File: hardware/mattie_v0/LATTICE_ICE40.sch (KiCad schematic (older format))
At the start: 4 parts

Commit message: update
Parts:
- gave numbers to parts that had none: 1
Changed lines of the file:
@@
 $Descr A4 11693 8268
 encoding utf-8
-Sheet 4 5
+Sheet 4 4
 Title "Mattie Version 0"
 Date ""
@@
 $EndDescr
 $Comp
-L FPGA_Lattice:ICE40UP5K-SG48ITR U?
+L FPGA_Lattice:ICE40UP5K-SG48ITR U2
 U 1 1 5E98B902
 P 3500 2300
-F 0 "U?" H 3830 2353 50  0000 L CNN
+F 0 "U2" H 3830 2353 50  0000 L CNN
 F 1 "ICE40UP5K-SG48ITR" H 3830 2262 50  0000 L CNN
 F 2 "Package_DFN_QFN:QFN-48-1EP_7x7mm_P0.5mm_EP5.6x5.6mm" H 3500 950 50  0001 C CNN
@@
 $EndComp
 $Comp
-L FPGA_Lattice:ICE40UP5K-SG48ITR U?
+L FPGA_Lattice:ICE40UP5K-SG48ITR U2
 U 2 1 5E98CFDA
 P 5550 2350
-F 0 "U?" H 5550 1275 50  0000 C CNN
+F 0 "U2" H 5550 1275 50  0000 C CNN
 F 1 "ICE40UP5K-SG48ITR" H 5550 1184 50  0000 C CNN
 F 2 "Package_DFN_QFN:QFN-48-1EP_7x7mm_P0.5mm_EP5.6x5.6mm" H 5550 1000 50  0001 C CNN
@@
 $EndComp
 $Comp
-L FPGA_Lattice:ICE40UP5K-SG48ITR U?
+L FPGA_Lattice:ICE40UP5K-SG48ITR U2
 U 3 1 5E98DA7F
 P 3450 4950
-F 0 "U?" H 3780 5053 50  0000 L CNN
+F 0 "U2" H 3780 5053 50  0000 L CNN
 F 1 "ICE40UP5K-SG48ITR" H 3780 4962 50  0000 L CNN
 F 2 "Package_DFN_QFN:QFN-48-1EP_7x7mm_P0.5mm_EP5.6x5.6mm" H 3450 3600 50  0001 C CNN
@@
 $EndComp
 $Comp
-L FPGA_Lattice:ICE40UP5K-SG48ITR U?
+L FPGA_Lattice:ICE40UP5K-SG48ITR U2
 U 4 1 5E98E441
 P 5450 4850
-F 0 "U?" V 5083 4850 50  0000 C CNN
+F 0 "U2" V 5083 4850 50  0000 C CNN
 F 1 "ICE40UP5K-SG48ITR" V 5174 4850 50  0000 C CNN
 F 2 "Package_DFN_QFN:QFN-48-1EP_7x7mm_P0.5mm_EP5.6x5.6mm" H 5450 3500 50  0001 C CNN

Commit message: some tweaks
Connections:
- net SPI_MISO: now reaches U2.14 (IOB_32a_SPI_SO)
- net SPI_SCK: now reaches U2.15 (IOB_34a_SPI_SCK)
- net SPI_SS: now reaches U2.16 (IOB_35b_SPI_SS)
- net SPI_MOSI: now reaches U2.17 (IOB_33b_SPI_SI)
- net DONE: now reaches U2.7 (CDONE)
- net RESET: now reaches U2.8 (~CRESET)
- net +1V2: now reaches U2.30 (VCC), U2.5 (VCC)
- net GND: now reaches U2.49 (GND)

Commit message: update
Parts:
- added C18, C19, C20, C21, C22, C23, C24: 0.1u, Capacitor_SMD:C_0603_1608Metric, symbol Device:C_Small
- added GPIO1: GPIO, Connector_PinHeader_2.54mm:PinHeader_2x06_P2.54mm_Vertical, symbol Connector_Generic:Conn_02x06_Odd_Even
- added U5: DSC1004, favorites:DSC1004, symbol favorites:DSC1004
- U2: footprint Package_DFN_QFN:QFN-48-1EP_7x7mm_P0.5mm_EP5.6x5.6mm -> Package_DFN_QFN:QFN-48-1EP_7x7mm_P0.5mm_EP5.45x5.45mm_ThermalVias
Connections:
- net +1V2: now also U2.29 (VCCPLL), C22.2, C24.2
- net AUX0: now also U2.19 (IOB_29b)
- net AUX1: now also U2.18 (IOB_31b)
- net AUX2: now also U2.45 (IOB_5b)
- net AUX3: now also U2.2 (IOB_6a)
- net AUX4: now also U2.28 (IOT_41a)
- net AUX5: now also U2.31 (IOT_42b)
- net DAT0: now also U2.6 (IOB_13b)
- net DAT1: now also U2.9 (IOB_16a)
- net DAT10: now also U2.44 (IOB_3b_G6)
- net DAT11: now also U2.48 (IOB_4a)
- net DAT12: now also U2.25 (IOT_36b)
- net DAT13: now also U2.23 (IOT_37a)
- net DAT14: now also U2.27 (IOT_38b)
- net DAT15: now also U2.26 (IOT_39a)
- net DAT2: now also U2.10 (IOB_18a)
- net DAT3: now also U2.11 (IOB_20a)
- net DAT4: now also U2.12 (IOB_22b)
- net DAT5: now also U2.21 (IOB_23b)
- net DAT6: now also U2.13 (IOB_24a)
- net DAT7: now also U2.20 (IOB_25b_G3)
- net DAT8: now also U2.46 (IOB_0a)
- net DAT9: now also U2.47 (IOB_2a)
- net GND: now also C18.2, C19.2, C20.2, C21.2, C22.1, C23.2, C24.1, U5.2 (GND)
- net IOT_43a: now reaches U2.32 (IOT_43a)
- net IOT_43a: now also GPIO1.1 (Pin_1)
- net +3V3: now reaches U2.33 (VCCIO_0)
- net +3V3: now also U2.1 (VCCIO_2), U2.22 (SPI_VCCIO1), U2.24 (VPP_2V5), C18.1, C19.1, C20.1, C21.1, C23.1, U5.1 (STNDBY), U5.4 (VDD)
- net IOT_44b: now reaches U2.34 (IOT_44b)
- net IOT_44b: now also GPIO1.2 (Pin_2)
- net CLK_100MHz: now reaches U2.35 (IOT_46b_G0)
- net CLK_100MHz: now also U5.3 (OUT)
- net IOT_48b: now reaches U2.36 (IOT_48b)
- net IOT_48b: now also GPIO1.4 (Pin_4)
- net IOT_45a: now reaches U2.37 (IOT_45a_G1)
- net IOT_45a: now also GPIO1.3 (Pin_3)
- net IOT_50b: now reaches U2.38 (IOT_50b)
- net IOT_50b: now also GPIO1.6 (Pin_6)
- net RGB0: now reaches U2.39 (RGB0)
- net RGB0: now also GPIO1.10 (Pin_10)
- net RGB1: now reaches U2.40 (RGB1)
- net RGB1: now also GPIO1.11 (Pin_11)
- net RGB2: now reaches U2.41 (RGB2)
- net RGB2: now also GPIO1.12 (Pin_12)
- net IOT_51a: now reaches U2.42 (IOT_51a)
- net IOT_51a: now also GPIO1.7 (Pin_7)
- net IOT_49a: now reaches U2.43 (IOT_49a)
- net IOT_49a: now also GPIO1.5 (Pin_5)
- net IOT_9b: now reaches U2.3 (IOB_9b)
- net IOT_9b: now also GPIO1.9 (Pin_9)
- net IOT_8a: now reaches U2.4 (IOB_8a)
- net IOT_8a: now also GPIO1.8 (Pin_8)

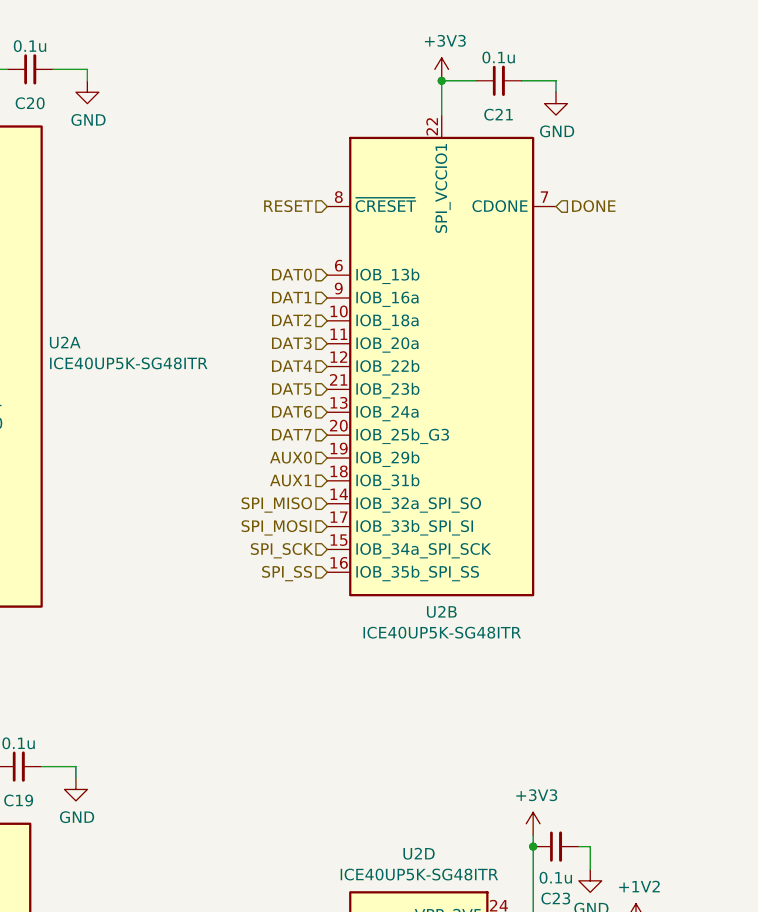
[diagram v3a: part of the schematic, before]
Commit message: added pullups and pulldowns
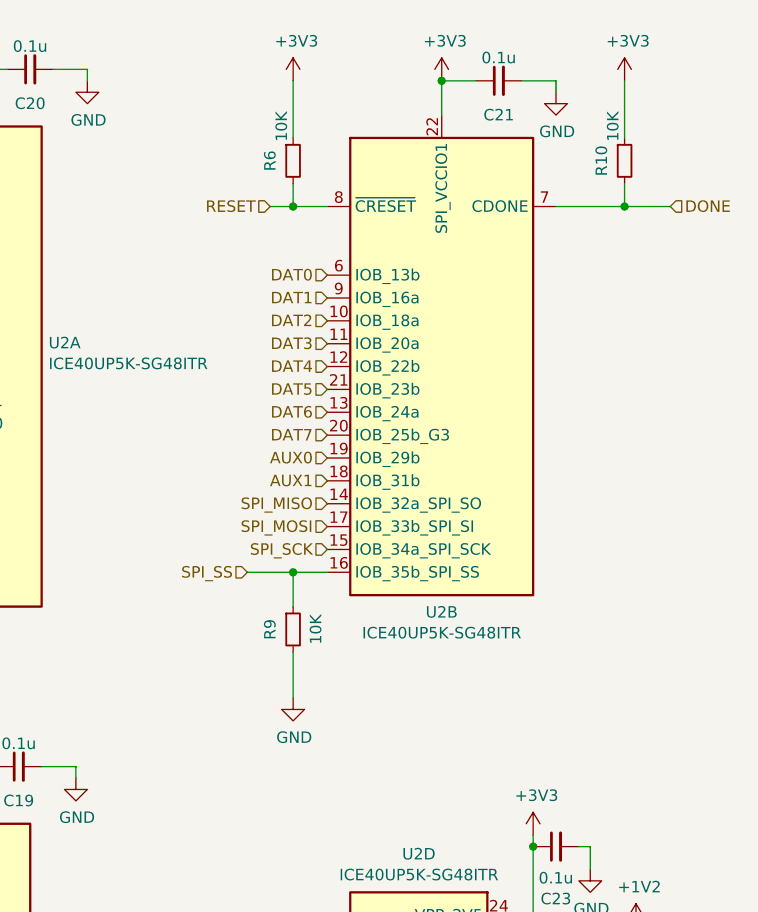
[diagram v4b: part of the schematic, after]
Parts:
- added R10, R6, R9: 10K, Resistor_SMD:R_0603_1608Metric, symbol Device:R_Small
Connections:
- net +3V3: now also R10.1, R6.1
- net DONE: now also R10.2
- net GND: now also R9.2
- net RESET: now also R6.2
- net SPI_SS: now also R9.1
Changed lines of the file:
@@
 	0    1    1    0
 $EndComp
-Text HLabel 5050 3250 0    50   Input ~ 0
+Text HLabel 4700 3250 0    50   Input ~ 0
 SPI_SS
 Text HLabel 5050 3150 0    50   Input ~ 0
@@
 Text HLabel 5050 3050 0    50   Input ~ 0
 SPI_MOSI
-Text HLabel 5050 1650 0    50   Input ~ 0
+Text HLabel 4800 1650 0    50   Input ~ 0
 RESET
-Text HLabel 6050 1650 2    50   Input ~ 0
+Text HLabel 6550 1650 2    50   Input ~ 0
 DONE
 Text HLabel 5050 1950 0    50   Input ~ 0
@@
 Wire Wire Line
 	1200 3750 1200 3600
+$Comp
+L Device:R_Small R?
+U 1 1 5EA31740
+P 4900 1450
+AR Path="/5E994520/5EA31740" Ref="R?"  Part="1"
+AR Path="/5E9881B4/5EA31740" Ref="R?"  Part="1"
+AR Path="/5E98823A/5EA31740" Ref="R6"  Part="1"
+F 0 "R6" V 4800 1450 50  0000 C CNN
+F 1 "10K" V 4850 1600 50  0000 C CNN
+F 2 "Resistor_SMD:R_0603_1608Metric" H 4900 1450 50  0001 C CNN
+F 3 "~" H 4900 1450 50  0001 C CNN
+F 4 " 71-CRCW060310K0JNEAC " H 4900 1450 50  0001 C CNN "OrderN"
+	1    4900 1450
+	1    0    0    -1
+$EndComp
+$Comp
+L power:+3V3 #PWR032
+U 1 1 5EA31EB6
+P 4900 1100
+F 0 "#PWR032" H 4900 950 50  0001 C CNN
+F 1 "+3V3" H 4915 1273 50  0000 C CNN
+F 2 "" H 4900 1100 50  0001 C CNN
+F 3 "" H 4900 1100 50  0001 C CNN
+	1    4900 1100
+	1    0    0    -1
+$EndComp
+Wire Wire Line
+	5050 1650 4900 1650
+Wire Wire Line
+	4900 1350 4900 1100
+Wire Wire Line
+	4900 1550 4900 1650
+Connection ~ 4900 1650
+Wire Wire Line
+	4900 1650 4800 1650
+$Comp
+L Device:R_Small R?
+U 1 1 5EA3656D
+P 6350 1450
+AR Path="/5E994520/5EA3656D" Ref="R?"  Part="1"
+AR Path="/5E9881B4/5EA3656D" Ref="R?"  Part="1"
+AR Path="/5E98823A/5EA3656D" Ref="R10"  Part="1"
+F 0 "R10" V 6250 1450 50  0000 C CNN
+F 1 "10K" V 6300 1600 50  0000 C CNN
+F 2 "Resistor_SMD:R_0603_1608Metric" H 6350 1450 50  0001 C CNN
+F 3 "~" H 6350 1450 50  0001 C CNN
+F 4 " 71-CRCW060310K0JNEAC " H 6350 1450 50  0001 C CNN "OrderN"
+	1    6350 1450
+	1    0    0    -1
+$EndComp
+$Comp
+L power:+3V3 #PWR034
+U 1 1 5EA3694D
+P 6350 1100
+F 0 "#PWR034" H 6350 950 50  0001 C CNN
+F 1 "+3V3" H 6365 1273 50  0000 C CNN
+F 2 "" H 6350 1100 50  0001 C CNN
+F 3 "" H 6350 1100 50  0001 C CNN
+	1    6350 1100
+	1    0    0    -1
+$EndComp
+Wire Wire Line
+	6050 1650 6350 1650
+Wire Wire Line
+	6350 1650 6350 1550
+Connection ~ 6350 1650
+Wire Wire Line
+	6350 1650 6550 1650
+Wire Wire Line
+	6350 1350 6350 1100
+$Comp
+L Device:R_Small R?
+U 1 1 5EA408B3
+P 4900 3500
+AR Path="/5E994520/5EA408B3" Ref="R?"  Part="1"
+AR Path="/5E9881B4/5EA408B3" Ref="R?"  Part="1"
+AR Path="/5E98823A/5EA408B3" Ref="R9"  Part="1"
+F 0 "R9" V 4800 3500 50  0000 C CNN
+F 1 "10K" V 5000 3500 50  0000 C CNN
+F 2 "Resistor_SMD:R_0603_1608Metric" H 4900 3500 50  0001 C CNN
+F 3 "~" H 4900 3500 50  0001 C CNN
+F 4 " 71-CRCW060310K0JNEAC " H 4900 3500 50  0001 C CNN "OrderN"
+	1    4900 3500
+	1    0    0    -1
+$EndComp
+$Comp
+L power:GND #PWR033
+U 1 1 5EA429FE
+P 4900 3800
+F 0 "#PWR033" H 4900 3550 50  0001 C CNN
+F 1 "GND" H 4905 3627 50  0000 C CNN
+F 2 "" H 4900 3800 50  0001 C CNN
+F 3 "" H 4900 3800 50  0001 C CNN
+	1    4900 3800
+	1    0    0    -1
+$EndComp
+Wire Wire Line
+	4900 3800 4900 3600
+Wire Wire Line
+	4900 3400 4900 3250
+Wire Wire Line
+	4900 3250 4700 3250
+Wire Wire Line
+	5050 3250 4900 3250
+Connection ~ 4900 3250
 $EndSCHEMATC

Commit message: tweaks
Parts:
- C18, C19, C20, C21, C22, C23, C24: Mouser 963-TMK107BJ104KA-T -> (none); OrderN (none) -> 963-TMK107BJ104KA-T
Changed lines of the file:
@@
 F 2 "Capacitor_SMD:C_0603_1608Metric" H 2500 3600 50  0001 C CNN
 F 3 "~" H 2500 3600 50  0001 C CNN
-F 4 " 963-TMK107BJ104KA-T " H 2500 3600 50  0001 C CNN "Mouser"
+F 4 "" H 2500 3600 50  0001 C CNN "Mouser"
+F 5 " 963-TMK107BJ104KA-T " H 2500 3600 50  0001 C CNN "OrderN"
 	1    2500 3600
 	0    -1   -1   0
@@
 F 2 "Capacitor_SMD:C_0603_1608Metric" H 6400 5000 50  0001 C CNN
 F 3 "~" H 6400 5000 50  0001 C CNN
-F 4 " 963-TMK107BJ104KA-T " H 6400 5000 50  0001 C CNN "Mouser"
+F 4 "" H 6400 5000 50  0001 C CNN "Mouser"
+F 5 " 963-TMK107BJ104KA-T " H 6400 5000 50  0001 C CNN "OrderN"
 	1    6400 5000
 	-1   0    0    1
@@
 F 2 "Capacitor_SMD:C_0603_1608Metric" H 6000 5050 50  0001 C CNN
 F 3 "~" H 6000 5050 50  0001 C CNN
-F 4 " 963-TMK107BJ104KA-T " H 6000 5050 50  0001 C CNN "Mouser"
+F 4 "" H 6000 5050 50  0001 C CNN "Mouser"
+F 5 " 963-TMK107BJ104KA-T " H 6000 5050 50  0001 C CNN "OrderN"
 	1    6000 5050
 	-1   0    0    1
@@
 F 2 "Capacitor_SMD:C_0603_1608Metric" H 6050 4450 50  0001 C CNN
 F 3 "~" H 6050 4450 50  0001 C CNN
-F 4 " 963-TMK107BJ104KA-T " H 6050 4450 50  0001 C CNN "Mouser"
+F 4 "" H 6050 4450 50  0001 C CNN "Mouser"
+F 5 " 963-TMK107BJ104KA-T " H 6050 4450 50  0001 C CNN "OrderN"
 	1    6050 4450
 	0    -1   -1   0
@@
 F 2 "Capacitor_SMD:C_0603_1608Metric" H 3700 4100 50  0001 C CNN
 F 3 "~" H 3700 4100 50  0001 C CNN
-F 4 " 963-TMK107BJ104KA-T " H 3700 4100 50  0001 C CNN "Mouser"
+F 4 "" H 3700 4100 50  0001 C CNN "Mouser"
+F 5 " 963-TMK107BJ104KA-T " H 3700 4100 50  0001 C CNN "OrderN"
 	1    3700 4100
 	0    -1   -1   0
@@
 F 2 "Capacitor_SMD:C_0603_1608Metric" H 3750 1050 50  0001 C CNN
 F 3 "~" H 3750 1050 50  0001 C CNN
-F 4 " 963-TMK107BJ104KA-T " H 3750 1050 50  0001 C CNN "Mouser"
+F 4 "" H 3750 1050 50  0001 C CNN "Mouser"
+F 5 " 963-TMK107BJ104KA-T " H 3750 1050 50  0001 C CNN "OrderN"
 	1    3750 1050
 	0    -1   -1   0
@@
 F 2 "Capacitor_SMD:C_0603_1608Metric" H 5800 1100 50  0001 C CNN
 F 3 "~" H 5800 1100 50  0001 C CNN
-F 4 " 963-TMK107BJ104KA-T " H 5800 1100 50  0001 C CNN "Mouser"
+F 4 "" H 5800 1100 50  0001 C CNN "Mouser"
+F 5 " 963-TMK107BJ104KA-T " H 5800 1100 50  0001 C CNN "OrderN"
 	1    5800 1100
 	0    -1   -1   0
